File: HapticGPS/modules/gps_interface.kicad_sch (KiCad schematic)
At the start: 0 parts

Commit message: save
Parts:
- added AE2: ANT-GNCP, Sadman_antenna:NT-GNCP-TH258L15, symbol Device:Antenna
- added C38: 10uF, Capacitor_SMD:C_0805_2012Metric, symbol Device:C
- added C39, C42: 100nF, Capacitor_SMD:C_0603_1608Metric, symbol Device:C
- added C40, C43: 33pF, Capacitor_SMD:C_0402_1005Metric, symbol Device:C
- added C41: 4.7uF, Capacitor_SMD:C_0603_1608Metric, symbol Device:C
- added C44: 220mF, sadman_power_passive:FC0H224ZFTBR24, symbol Device:C
- added C45, C46: 2pF, Capacitor_SMD:C_0402_1005Metric, symbol Device:C
- added D2, D3: TVS, Diode_SMD:D_0402_1005Metric, symbol Device:D_Zener
- added D4: 1N4148WT, Diode_SMD:D_SOD-523, symbol Diode:1N4148WT
- added D5: TVS, Diode_SMD:D_0201_0603Metric, symbol Device:D_Zener
- added D6: YELLOW, Diode_SMD:D_0402_1005Metric, symbol Device:LED
- added L9: 6nH, Inductor_SMD:L_0402_1005Metric, symbol Device:L
- added Q1: RU1J002, Package_TO_SOT_SMD:SOT-323_SC-70, symbol Transistor_FET_Other:Q_NMOS_Depletion_GSD
- added R12: 1k, Resistor_SMD:R_0603_1608Metric, symbol Device:R
- added R14, R17, R18: 2.2k, Capacitor_SMD:C_0603_1608Metric, symbol Device:R
- added R15: 100K, Resistor_SMD:R_0603_1608Metric, symbol Device:R
- added R16: 75, Resistor_SMD:R_0603_1608Metric, symbol Device:R
- added U5: LC29H, Sadman_RF_receivers:LC29H, symbol Sadman_RF_receiver:LC29HAA
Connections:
- new net: C45.1, L9.1, U5.11 (RF_IN)
- new net: Q1.3 (D), R16.1
- new net: D6.1 (K), R16.2
- new net: AE2.1 (A), C46.1, D5.1 (K), L9.2
- new net: Q1.1 (G), R14.2, R15.1
- new net: D4.1 (K), R12.1
- new net: R14.1, U5.3 (1PPS)
- new net GND: C38.2, C39.2, C40.2, C41.1, C42.2, C43.2, C44.2, C45.2, C46.2, D2.2 (A), D3.2 (A), D5.2 (A), Q1.2 (S), R15.2, R17.2, R18.2, U5.10 (GND), U5.12 (GND), U5.13 (GND), U5.24 (GND)
- new net NRST_GPS: R18.1, U5.8 (RESET_N)
- new net RX_GPS: U5.21 (RXD)
- new net TX_GPS: U5.20 (TXD)
- new net VBACKUP_GPS: C41.2, C42.1, C43.1, C44.1, D3.1 (K), R12.2, U5.22 (V_BCKP)
- new net VIN_GPS: C38.1, C39.1, C40.1, D2.1 (K), D4.2 (A), D6.2 (A), U5.23 (VCC)
- new net WKUP_GPS: R17.1, U5.1 (WAKE_UP)
- no-connect marks 0 -> 5

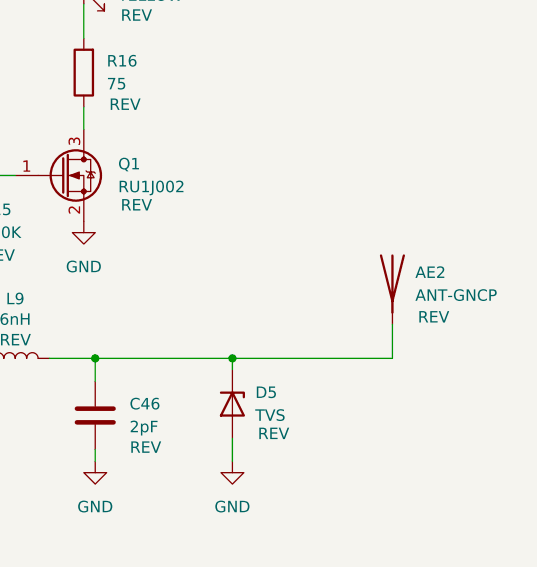
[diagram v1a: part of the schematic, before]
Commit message: eliminating GPS, and second piezo driver
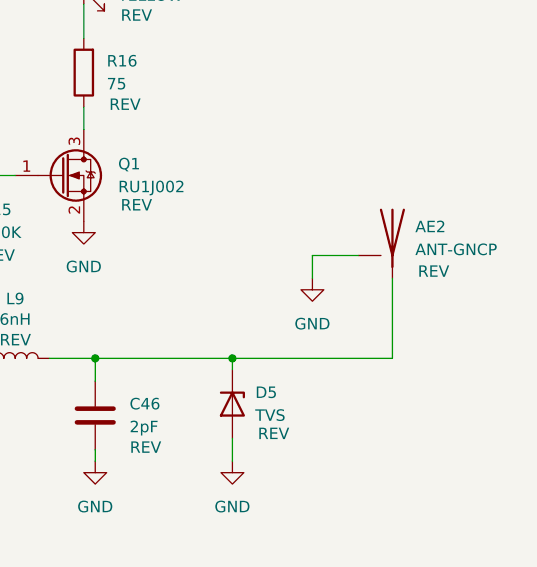
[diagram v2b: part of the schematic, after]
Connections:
- net GND: now also AE2.2 (GND)
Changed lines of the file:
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@@
 	(wire
 		(pts
-			(xy 250.19 74.93) (xy 250.19 71.12)
+			(xy 250.19 74.93) (xy 250.19 66.04)
 		)
 		(stroke
@@
 	(wire
 		(pts
+			(xy 246.38 63.5) (xy 241.3 63.5)
+		)
+		(stroke
+			(width 0)
+			(type default)
+		)
+	)
+	(wire
+		(pts
 			(xy 198.12 74.93) (xy 204.47 74.93)
 		)
@@
 		(pts
 			(xy 105.41 64.77) (xy 105.41 63.5)
+		)
+		(stroke
+			(width 0)
+			(type default)
+		)
+	)
+	(wire
+		(pts
+			(xy 241.3 63.5) (xy 241.3 66.04)
 		)
 		(stroke
@@
 	)
 	(symbol
+		(lib_id "power:GND")
+		(at 241.3 66.04 0)
+		(unit 1)
+		(exclude_from_sim no)
+		(in_bom yes)
+		(on_board yes)
+		(dnp no)
+		(fields_autoplaced yes)
+		(property "Reference" "#PWR04"
+			(at 241.3 72.39 0)
+			(effects
+				(font
+					(size 1.27 1.27)
+				)
+				(hide yes)
+			)
+		)
+		(property "Value" "GND"
+			(at 241.3 71.12 0)
+			(effects
+				(font
+					(size 1.27 1.27)
+				)
+			)
+		)
+		(property "Footprint" ""
+			(at 241.3 66.04 0)
+			(effects
+				(font
+					(size 1.27 1.27)
+				)
+				(hide yes)
+			)
+		)
+		(property "Datasheet" ""
+			(at 241.3 66.04 0)
+			(effects
+				(font
+					(size 1.27 1.27)
+				)
+				(hide yes)
+			)
+		)
+		(property "Description" "Power symbol creates a global label with name \"GND\" , ground"
+			(at 241.3 66.04 0)
+			(effects
+				(font
+					(size 1.27 1.27)
+				)
+				(hide yes)
+			)
+		)
+		(pin "1"
+		)
+		(instances
+			(project "HapticGPS"
+				(path "/429dbf39-a1a7-452e-94e3-b1241e04beaa/4cb5cc37-6dd4-4cc6-8dfa-25cbabfac881"
+					(reference "#PWR04")
+					(unit 1)
+				)
+			)
+		)
+	)
+	(symbol
 		(lib_id "Device:Antenna")
-		(at 250.19 66.04 0)
+		(at 250.19 60.96 0)
 		(unit 1)
 		(exclude_from_sim no)
@@
 		(dnp no)
 		(property "Reference" "AE2"
-			(at 252.73 65.4049 0)
+			(at 252.73 60.3249 0)
 			(effects
 				(font
@@
 		)
 		(property "Value" "ANT-GNCP"
-			(at 252.73 67.9449 0)
+			(at 252.73 62.8649 0)
 			(effects
 				(font
@@
 		)
 		(property "Footprint" "Sadman_antenna:NT-GNCP-TH258L15"
-			(at 250.19 66.04 0)
+			(at 250.19 60.96 0)
 			(effects
 				(font
@@
 		)
 		(property "Datasheet" "https://www.digikey.es/es/products/detail/te-connectivity-linx/ant-gncp-th258l15/13627260#:~:text=base-,ANT%2DGNCP"
-			(at 250.19 66.04 0)
+			(at 250.19 60.96 0)
 			(effects
 				(font
@@
 		)
 		(property "Description" "RF ANT GNSS PATCH L1 L5 25MM PIN"
-			(at 250.19 66.04 0)
+			(at 250.19 60.96 0)
 			(effects
 				(font
@@
 		)
 		(property "Manufacturer" "TE Connectivity Linx"
-			(at 250.19 66.04 0)
+			(at 250.19 60.96 0)
 			(effects
 				(font
@@
 		)
 		(property "Number Part" "ANT-GNCP-TH258L15"
-			(at 250.19 66.04 0)
+			(at 250.19 60.96 0)
 			(effects
 				(font
@@
 		)
 		(property "Provider" "Digikey"
-			(at 250.19 66.04 0)
+			(at 250.19 60.96 0)
 			(effects
 				(font
@@
 		)
 		(property "Revisado" "REV"
-			(at 254.762 70.358 0)
+			(at 254.762 65.278 0)
 			(effects
 				(font
@@
 		)
 		(property "Voltage" ""
-			(at 250.19 66.04 0)
+			(at 250.19 60.96 0)
 			(effects
 				(font
@@
 		(pin "1"
 		)
+		(pin "2"
+		)
 		(instances
